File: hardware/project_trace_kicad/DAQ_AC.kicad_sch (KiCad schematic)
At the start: 52 parts, among them U301 THS4131IDR, U303 ADS1602, U304 MCP6499T, U305 LM4040DBZ-2.5, U306 LM4040DBZ-4.1

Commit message: Layout Broad Strokes, Fix STM32H7 Error
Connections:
- net +1V0: now also U304.1, U304.2 (-); no longer U304.13 (-), U304.14
- net +4V: now also U304.13 (-), U304.14; no longer U304.1, U304.2 (-)
- net at R313.2, R314.1: now also U304.3 (+); no longer U304.12 (+)
- net at R312.1, R317.2: now also U304.12 (+); no longer U304.3 (+)
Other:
- moved on the sheet: U304A, U304D
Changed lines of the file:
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@@
 	)
 	(junction
-		(at 252.73 102.87)
-		(diameter 0)
-		(color 0 0 0 0)
-	)
-	(junction
 		(at 243.84 140.97)
 		(diameter 0)
@@
 	(wire
 		(pts
-			(xy 252.73 102.87) (xy 252.73 104.14)
-		)
-		(stroke
-			(width 0)
-			(type default)
-		)
-	)
-	(wire
-		(pts
 			(xy 226.06 143.51) (xy 226.06 148.59)
 		)
@@
 	(symbol
 		(lib_id "ProjectTraceSymbols:MCP6499T")
-		(at 264.16 95.25 0)
+		(at 270.51 151.13 0)
 		(unit 4)
 		(body_style 1)
@@
 		(fields_autoplaced yes)
 		(property "Reference" "U304"
-			(at 264.16 86.4106 0)
+			(at 270.51 142.2906 0)
 			(show_name no)
 			(do_not_autoplace no)
@@
 		)
 		(property "Value" "MCP6499T"
-			(at 264.16 88.5782 0)
+			(at 270.51 144.4582 0)
 			(show_name no)
 			(do_not_autoplace no)
@@
 		)
 		(property "Footprint" "ProjectTraceFootprints:SOIC-14_3.9x8.7mm_P1.27mm_Handsolder"
-			(at 262.89 92.71 0)
+			(at 269.24 148.59 0)
 			(hide yes)
 			(show_name no)
@@
 		)
 		(property "Datasheet" "http://www.ti.com/lit/ds/symlink/lm2902-n.pdf"
-			(at 265.43 90.17 0)
+			(at 271.78 146.05 0)
 			(hide yes)
 			(show_name no)
@@
 		)
 		(property "Description" "Low-Power, Quad-Operational Amplifiers, DIP-14/SOIC-14/SSOP-14"
-			(at 264.16 95.25 0)
+			(at 270.51 151.13 0)
 			(hide yes)
 			(show_name no)
@@
 		)
 		(property "DigikeyPN" "150-MCP6499T-E/SLCT-ND"
-			(at 264.16 95.25 0)
+			(at 270.51 151.13 0)
 			(hide yes)
 			(show_name no)
@@
 	(symbol
 		(lib_id "ProjectTraceSymbols:MCP6499T")
-		(at 270.51 151.13 0)
+		(at 264.16 95.25 0)
 		(unit 1)
 		(body_style 1)
@@
 		(fields_autoplaced yes)
 		(property "Reference" "U304"
-			(at 270.51 142.2906 0)
+			(at 264.16 86.4106 0)
 			(show_name no)
 			(do_not_autoplace no)
@@
 		)
 		(property "Value" "MCP6499T"
-			(at 270.51 144.4582 0)
+			(at 264.16 88.5782 0)
 			(show_name no)
 			(do_not_autoplace no)
@@
 		)
 		(property "Footprint" "ProjectTraceFootprints:SOIC-14_3.9x8.7mm_P1.27mm_Handsolder"
-			(at 269.24 148.59 0)
+			(at 262.89 92.71 0)
 			(hide yes)
 			(show_name no)
@@
 		)
 		(property "Datasheet" "http://www.ti.com/lit/ds/symlink/lm2902-n.pdf"
-			(at 271.78 146.05 0)
+			(at 265.43 90.17 0)
 			(hide yes)
 			(show_name no)
@@
 		)
 		(property "Description" "Low-Power, Quad-Operational Amplifiers, DIP-14/SOIC-14/SSOP-14"
-			(at 270.51 151.13 0)
+			(at 264.16 95.25 0)
 			(hide yes)
 			(show_name no)
@@
 		)
 		(property "DigikeyPN" "150-MCP6499T-E/SLCT-ND"
-			(at 270.51 151.13 0)
+			(at 264.16 95.25 0)
 			(hide yes)
 			(show_name no)

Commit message: Add missing Part-numers, Revise AC Coupling
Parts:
- C309, C310, C311: DigikeyPN (none) -> 311-1069-1-ND
- R304, R305: DigikeyPN (none) -> YAG1638CT-ND
- R306, R307: DigikeyPN (none) -> YAG1237CT-ND
- R308, R309: DigikeyPN (none) -> YAG4511CT-ND
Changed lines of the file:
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@@
 			)
 		)
+		(property "DigikeyPN" "YAG1237CT-ND"
+			(at 99.06 71.12 90)
+			(hide yes)
+			(show_name no)
+			(do_not_autoplace no)
+			(effects
+				(font
+					(size 1.27 1.27)
+				)
+			)
+		)
 		(pin "1"
 		)
@@
 			)
 		)
+		(property "DigikeyPN" "YAG1638CT-ND"
+			(at 86.36 71.12 90)
+			(hide yes)
+			(show_name no)
+			(do_not_autoplace no)
+			(effects
+				(font
+					(size 1.27 1.27)
+				)
+			)
+		)
 		(pin "1"
 		)
@@
 			)
 		)
+		(property "DigikeyPN" "YAG1237CT-ND"
+			(at 99.06 44.45 90)
+			(hide yes)
+			(show_name no)
+			(do_not_autoplace no)
+			(effects
+				(font
+					(size 1.27 1.27)
+				)
+			)
+		)
 		(pin "1"
 		)
@@
 			)
 		)
+		(property "DigikeyPN" "YAG4511CT-ND"
+			(at 118.11 44.45 90)
+			(hide yes)
+			(show_name no)
+			(do_not_autoplace no)
+			(effects
+				(font
+					(size 1.27 1.27)
+				)
+			)
+		)
 		(pin "1"
 		)
@@
 			)
 		)
+		(property "DigikeyPN" "YAG1638CT-ND"
+			(at 86.36 44.45 90)
+			(hide yes)
+			(show_name no)
+			(do_not_autoplace no)
+			(effects
+				(font
+					(size 1.27 1.27)
+				)
+			)
+		)
 		(pin "1"
 		)
@@
 			)
 		)
+		(property "DigikeyPN" "311-1069-1-ND"
+			(at 127 77.47 0)
+			(hide yes)
+			(show_name no)
+			(do_not_autoplace no)
+			(effects
+				(font
+					(size 1.27 1.27)
+				)
+			)
+		)
 		(pin "1"
 		)
@@
 			)
 		)
+		(property "DigikeyPN" "YAG4511CT-ND"
+			(at 119.38 71.12 90)
+			(hide yes)
+			(show_name no)
+			(do_not_autoplace no)
+			(effects
+				(font
+					(size 1.27 1.27)
+				)
+			)
+		)
 		(pin "1"
 		)
@@
 			)
 		)
+		(property "DigikeyPN" "311-1069-1-ND"
+			(at 127 58.42 0)
+			(hide yes)
+			(show_name no)
+			(do_not_autoplace no)
+			(effects
+				(font
+					(size 1.27 1.27)
+				)
+			)
+		)
 		(pin "1"
 		)
@@
 			)
 		)
+		(property "DigikeyPN" "311-1069-1-ND"
+			(at 127 39.37 0)
+			(hide yes)
+			(show_name no)
+			(do_not_autoplace no)
+			(effects
+				(font
+					(size 1.27 1.27)
+				)
+			)
+		)

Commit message: Address Review Comments
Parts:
- removed C330: 220u, symbol Device:C_Polarized
- removed R312: 249, Resistor_SMD:R_0603_1608Metric_Pad0.98x0.95mm_HandSolder, symbol Device:R
- removed R313, R317: 10k, Resistor_SMD:R_0603_1608Metric_Pad0.98x0.95mm_HandSolder, symbol Device:R
- removed R314: 15k, Resistor_SMD:R_0603_1608Metric_Pad0.98x0.95mm_HandSolder, symbol Device:R
- removed U305: LM4040DBZ-2.5, Package_TO_SOT_SMD:SOT-23_Handsoldering, symbol Reference_Voltage:LM4040DBZ-2.5
- added RV301, RV302, RV303: 10k, Potentiometer_THT:Potentiometer_Bourns_3266W_Vertical, symbol Device:R_Potentiometer_Trim
- added TP302, TP303, TP304: TestPoint, TestPoint:TestPoint_Pad_1.5x1.5mm, symbol Connector:TestPoint
- C328, C329: footprint (none) -> Capacitor_THT:CP_Radial_D6.3mm_P2.50mm
- R310: value 37k -> 47k; footprint Resistor_SMD:R_0603_1608Metric_Pad0.98x0.95mm_HandSolder -> Resistor_THT:R_Axial_DIN0207_L6.3mm_D2.5mm_P10.16mm_Horizontal; DigikeyPN 2019-RN73R1JTTD3702F100CT-ND -> N/A
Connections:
- net +1V0: now also TP304.1
- net +2V5: now also TP303.1
- net +4V: now also TP302.1
- net +5V: no longer R310.1
- net 4V1: now also RV301.1, RV302.1, RV303.1
- net GND: now also R310.1, RV302.3, RV303.3
- net at R310.2: now also RV301.3; no longer U304.5 (+)
- net at U304.3 (+): now also RV303.2
- net at U304.12 (+): now also RV301.2
- new net: RV302.2, U304.5 (+)
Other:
- note added: "Power Symbols"
- note added: "Signal Path"
- note added: "TODO: Check Trim-Potentiometer Footprint with real component"
- note added: "Voltage Reference"
- moved on the sheet: C301, C302, C304, C305, C306, C307, C308, C309, C310, C311, C312, C313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

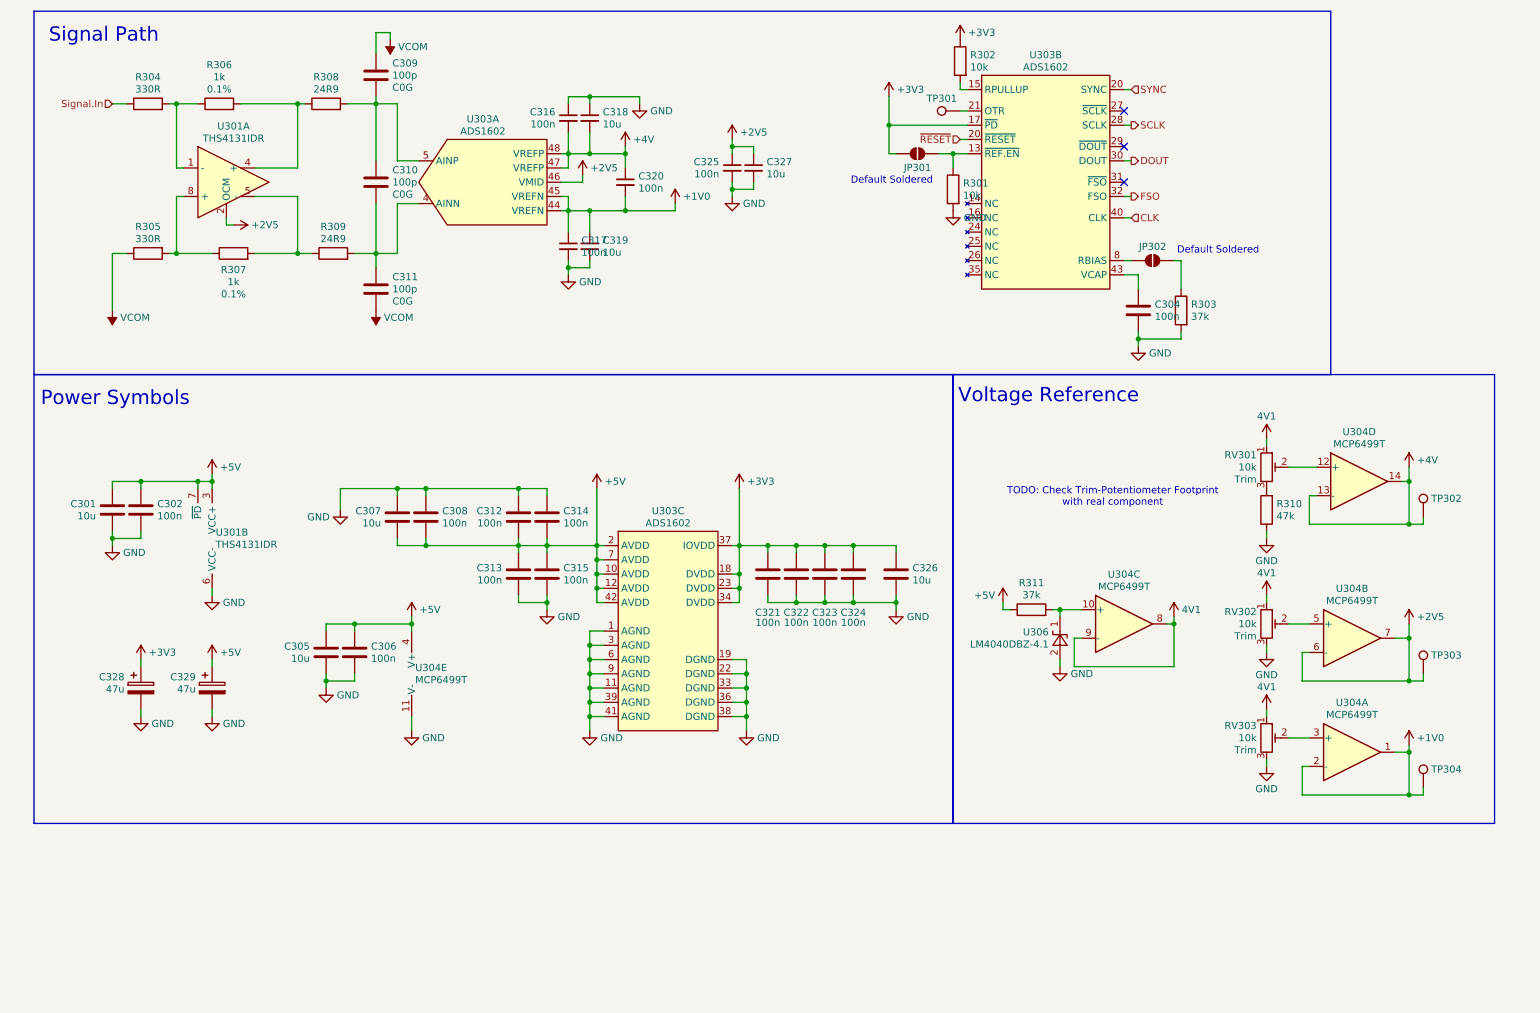
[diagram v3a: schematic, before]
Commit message: UI updated, CLK implemented, Parts labeled as Donotplace in power
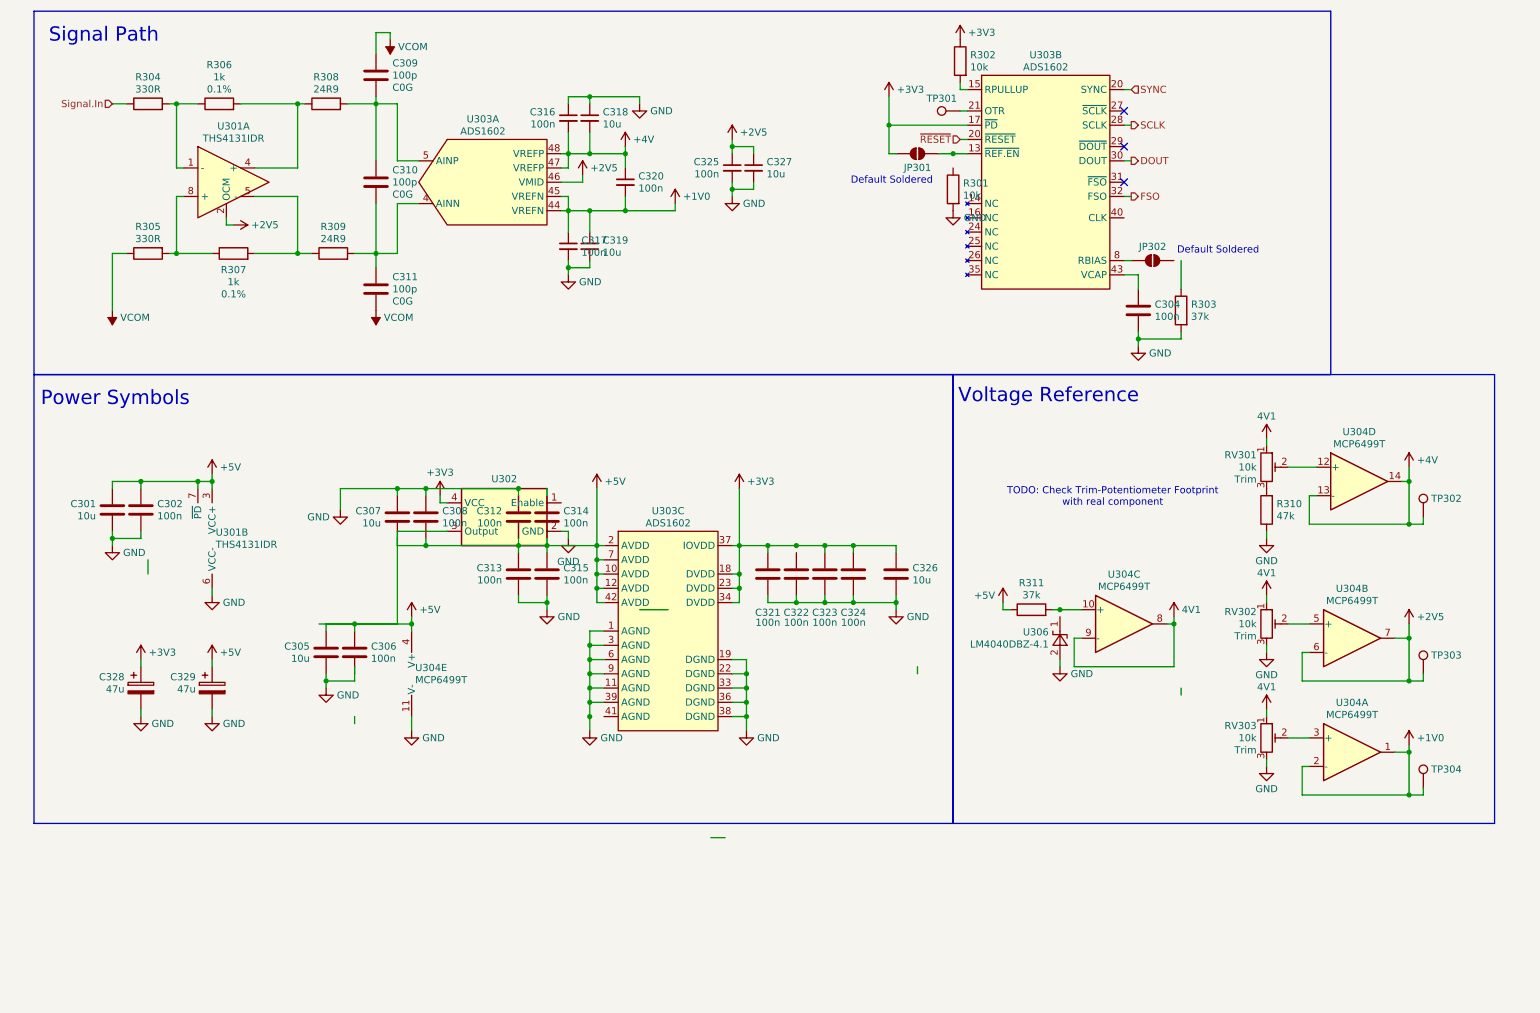
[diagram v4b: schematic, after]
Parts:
- added U302: (no value), ProjectTraceFootprints:IC_625L3C040M00000_CTS-M, symbol ProjectTraceSymbols:625L3C040M00000
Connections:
- net +3V3: now also U302.4 (VCC); no longer C322.2
- net +5V: now also U302.3 (Output)
- net GND: now also U302.2 (GND); no longer C314.2, U303.41 (AGND)
- net at JP301.1 (A), U303.13 (~{REF.EN}): no longer R301.1
- net at R311.2, U304.10 (+): no longer U306.1 (K)
- net at R303.1: no longer JP302.1 (A)
- net CLK: no longer names the net of U303.40 (CLK)

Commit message: Fix main-merge
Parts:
- added C303: 100n, Capacitor_SMD:C_0603_1608Metric_Pad1.08x0.95mm_HandSolder, symbol Device:C
- added JP303: SolderJumper_2_Open, Jumper:SolderJumper-2_P1.3mm_Open_RoundedPad1.0x1.5mm, symbol Jumper:SolderJumper_2_Open
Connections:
- net +3V3: now also C303.2
- net +5V: no longer U302.3 (Output)
- net GND: now also C314.2, C303.1
- net at JP301.1 (A), U303.13 (~{REF.EN}): now also R301.1
- net CLK.EN: now reaches U302.1 (Enable)
- net at R303.1: now also JP302.1 (A)
- net at U303.40 (CLK): now also U302.3 (Output), JP303.2 (B)
- new net CLK.BAC: JP303.1 (A)
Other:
- moved on the sheet: U302

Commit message: Before using stashed changes
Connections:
- net GND: now also U303.41 (AGND)
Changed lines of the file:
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@@
+	)
+	(junction
+		(at 118.11 143.51)
+		(diameter 0)
+		(color 0 0 0 0)
 	)
 	(junction
@@
 	(wire
 		(pts
-			(xy 76.2 134.62) (xy 76.2 135.89)
+			(xy 118.11 143.51) (xy 120.65 143.51)
 		)
 		(stroke
@@
 	(wire
 		(pts
-			(xy 118.11 140.97) (xy 118.11 146.05)
+			(xy 118.11 140.97) (xy 118.11 143.51)
 		)
 		(stroke
@@
 		)
 		(stroke
+			(width 0)
+			(type default)
+		)
+	)
+	(wire
+		(pts
+			(xy 118.11 143.51) (xy 118.11 146.05)
+		)
+		(stroke

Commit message: Updates to PCB, Schematic Fixes
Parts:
- R304, R305: Extra (none) -> 0.1%
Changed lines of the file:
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@@
 		(fields_autoplaced yes)
 		(property "Reference" "R305"
-			(at 39.37 56.1846 90)
+			(at 39.37 54.017 90)
 			(show_name no)
 			(do_not_autoplace no)
@@
 		)
 		(property "Value" "330R"
-			(at 39.37 58.3522 90)
+			(at 39.37 56.1846 90)
 			(show_name no)
 			(do_not_autoplace no)
@@
 			)
 		)
+		(property "Extra" "0.1%"
+			(at 39.37 58.3522 90)
+			(show_name no)
+			(do_not_autoplace no)
+			(effects
+				(font
+					(size 1.27 1.27)
+				)
+			)
+		)
 		(pin "1"
 		)
@@
 		(fields_autoplaced yes)
 		(property "Reference" "R304"
-			(at 39.37 29.5146 90)
+			(at 39.37 27.347 90)
 			(show_name no)
 			(do_not_autoplace no)
@@
 		)
 		(property "Value" "330R"
-			(at 39.37 31.6822 90)
+			(at 39.37 29.5146 90)
 			(show_name no)
 			(do_not_autoplace no)
@@
 			)
 		)
+		(property "Extra" "0.1%"
+			(at 39.37 31.6822 90)
+			(show_name no)
+			(do_not_autoplace no)
+			(effects
+				(font
+					(size 1.27 1.27)
+				)
+			)
+		)
 		(pin "1"
 		)
@@
 		(lib_id "Device:C_Small")
 		(at 114.3 59.69 0)
+		(mirror y)
 		(unit 1)
 		(body_style 1)
@@
 		(in_pos_files yes)
 		(dnp no)
-		(fields_autoplaced yes)
 		(property "Reference" "C317"
-			(at 116.6241 58.6125 0)
+			(at 111.9759 58.6125 0)
 			(show_name no)
 			(do_not_autoplace no)
@@
 		)
 		(property "Value" "100n"
-			(at 116.6241 60.7801 0)
+			(at 111.9759 60.7801 0)
 			(show_name no)
 			(do_not_autoplace no)
